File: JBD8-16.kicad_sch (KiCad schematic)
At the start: 54 parts, among them J1 RS232, J2 5V, SW1 RESET, U1 W65C02SxP, U10 CY62256-70PC(RAM), U10X 74LS32, U11 CY62256-70PC(RAM), U11X 74LS32, U12 CY62256-70PC(RAM), U12X 74LS04, U13 CY62256-70PC(RAM), U13X 74LS08, U14 CY62256-70PC(RAM), U14X 74LS11, U15 CY62256-70PC(RAM), U15X 74LS08, U16 CY62256-70PC(RAM), U16X 74LS11, U17X 74LS32, U18X 74LS11, U19X 74LS32, U1X 74LS154, U20X 74LS32, U2X 74LS154, U3 28C256(ROM), U3X 74LS154, U4 6522, U4 CY62256-70PC(RAM), U4X 74LS154, U5 W65C51NxP, U5X 74LS08, U6 MAX232, U6X 74LS32, U7X 74LS11, U8 74LS373, U8X 74LS32, U9 74LS138, U9X 74LS00, X1 1Mhz, Y1 1.8432Mhz

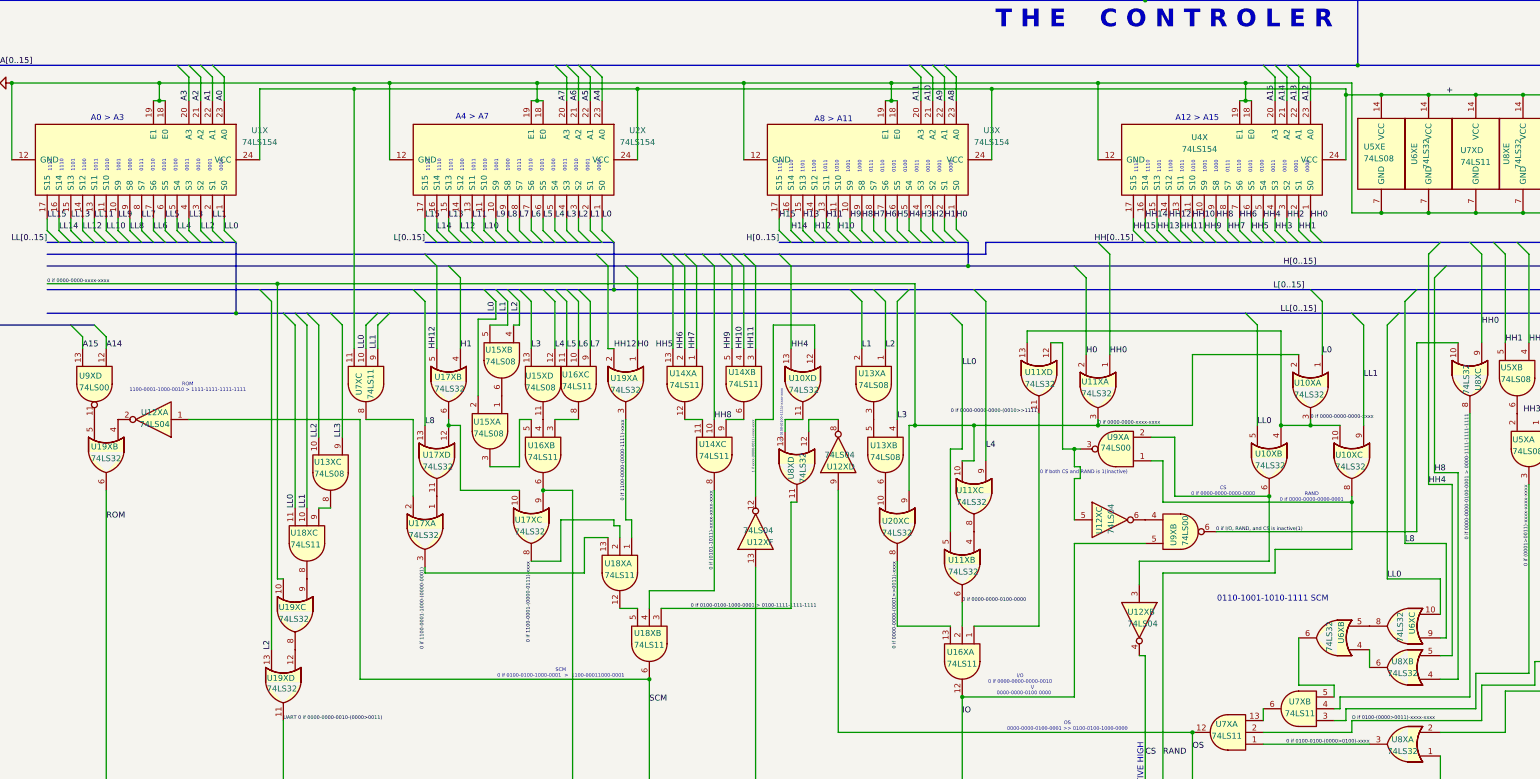
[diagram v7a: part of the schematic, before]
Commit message: Little bits of optimasition in decoder layout
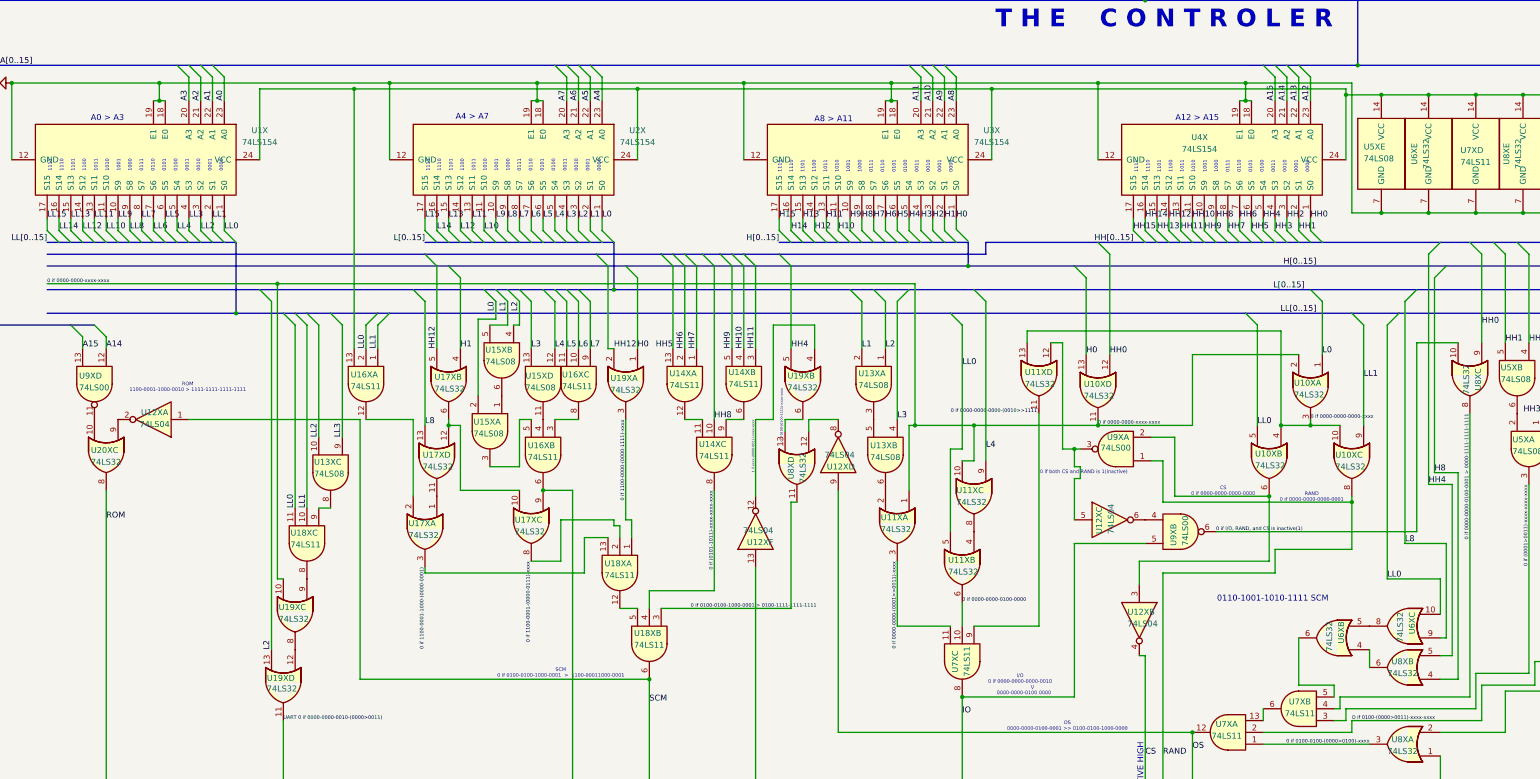
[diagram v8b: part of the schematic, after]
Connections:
- net +5V: now also U16X.13; no longer U7X.11
- net 0 if 0000-0000-(0001>>0011)-xxxx: now also U11X.3, U7X.11; no longer U16X.13, U20X.8
- net 0 if 0000-0000-0000-(0010>>1111): now also U7X.9; no longer U16X.1
- net 0 if 0000-0000-0100-0000: now also U7X.10; no longer U16X.2
- net 0 if 0000-0000-xxxx-xxxx: now also U10X.11, U11X.1; no longer U11X.3, U20X.9
- net 1 if xxxx-(0000-0011)-xxxx-xxxx: now also U19X.4; no longer U10X.12
- net H0: now also U10X.13; no longer U11X.2
- net HH0: now also U10X.12; no longer U11X.1
- net HH4: now also U19X.5; no longer U10X.13
- net IO: now also U7X.8; no longer U16X.12
- net LL0: now also U16X.2; no longer U7X.10
- net LL1: now also U16X.1; no longer U7X.9
- net ROM: now also U20X.8; no longer U19X.6
- net at U8X.13: now also U19X.6; no longer U10X.11
- net at U17X.2: now also U16X.12; no longer U7X.8
- net at U9X.11: now also U20X.10; no longer U19X.5
- net at U12X.2: now also U20X.9; no longer U19X.4
- net at U13X.6: now also U11X.2; no longer U20X.10
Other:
- moved on the sheet: U10XD, U11XA, U16XA, U19XB, U20XC, U7XC
